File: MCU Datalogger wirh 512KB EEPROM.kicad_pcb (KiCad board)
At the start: 2 copper layers, 56.3 x 48.7 mm, 30 parts, among them IC1 ATMEGA328P-AU, J1 Conn_01x04_Pin, J2 Conn_01x04_Pin, J3 Conn_01x09_Pin, J4 Conn_02x03_Odd_Even, U1 24LC1025, U2 24LC1025, U3 DS1137S+, Y1 16 MHz, Y2 32.768 KHz

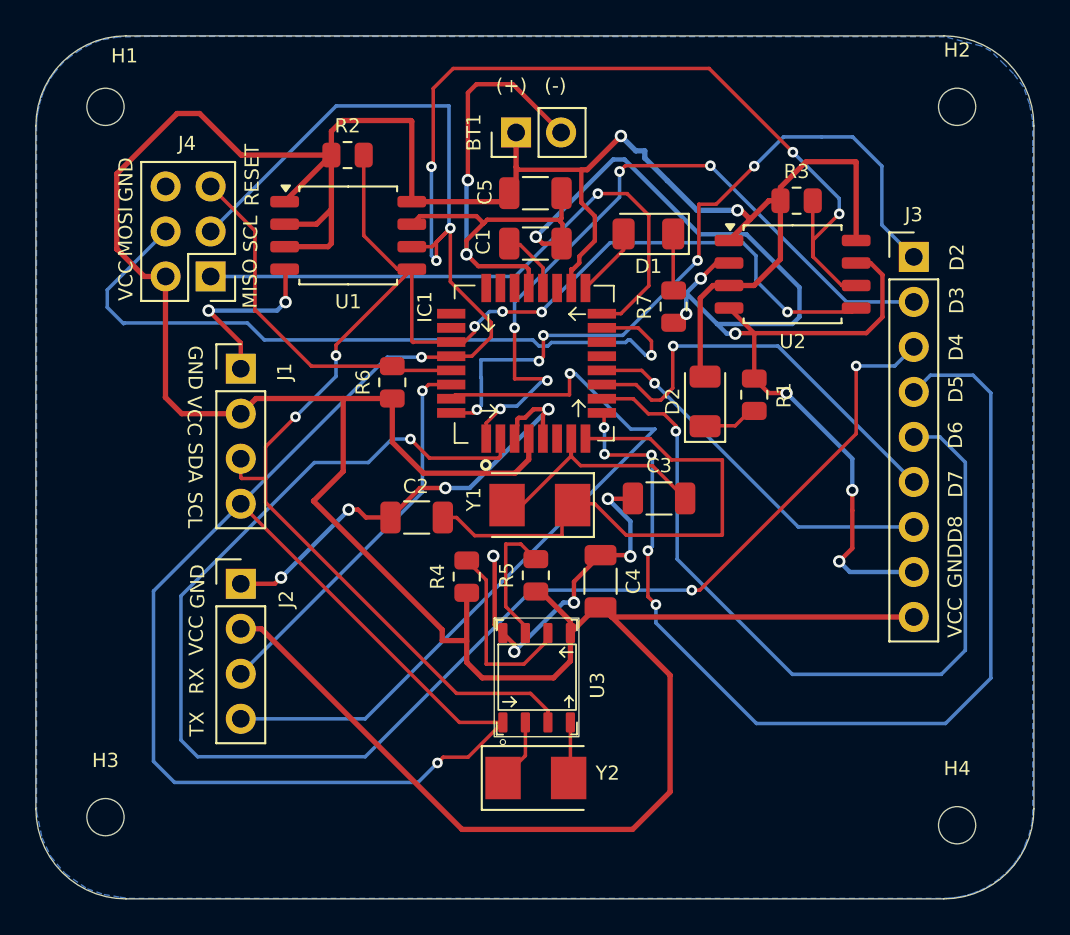
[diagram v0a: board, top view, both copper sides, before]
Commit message: Included values for assembly.
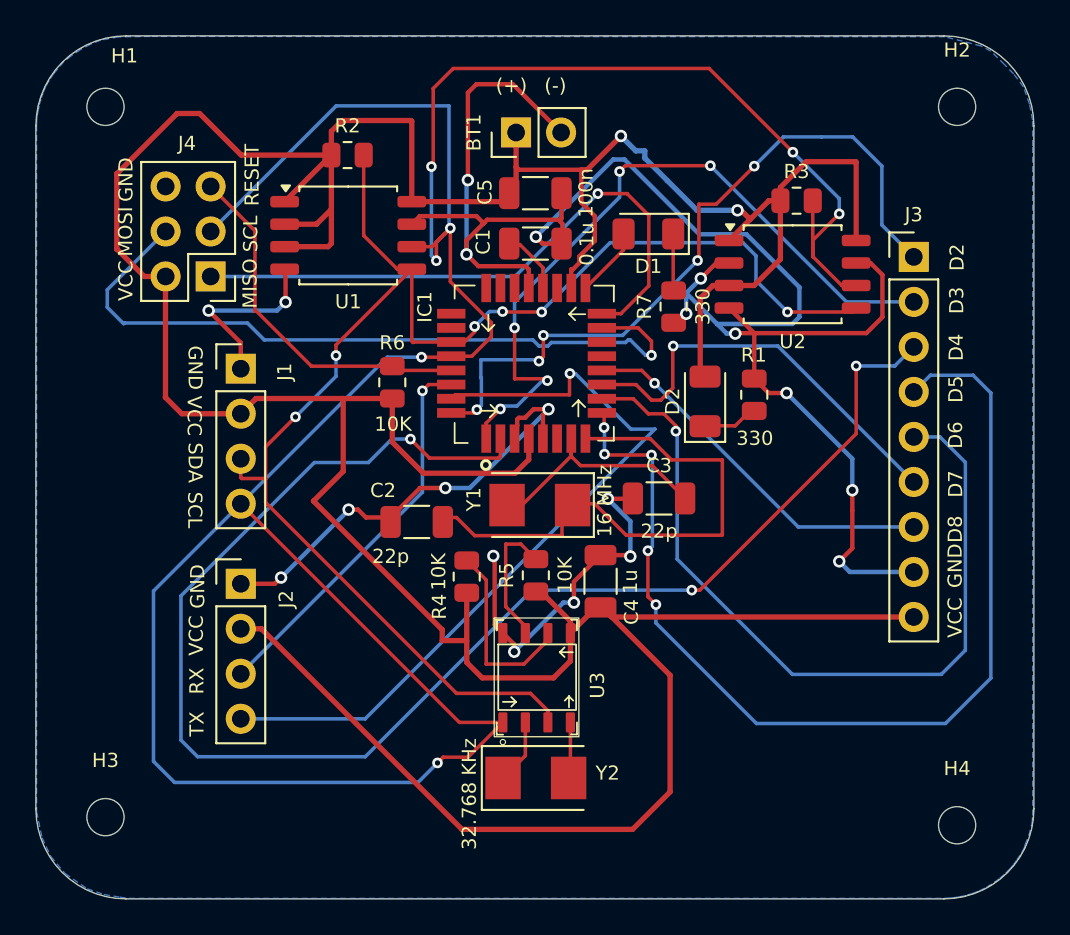
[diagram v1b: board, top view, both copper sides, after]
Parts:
- moved C2 0.25 mm to (129.2, 102.1)
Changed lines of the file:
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@@
 		)
 		(property "Value" "100n"
-			(at 0 1.85 0)
-			(layer "F.Fab")
+			(at 2.8515 -0.0171 90)
+			(layer "F.SilkS")
 			(effects
 				(font
-					(size 1 1)
+					(size 0.8 0.8)
 					(thickness 0.15)
 				)
@@
 		)
 		(property "Value" "16 MHz"
-			(at 0 2.8 0)
-			(layer "F.Fab")
+			(at -3.6615 0.2371 90)
+			(layer "F.SilkS")
 			(effects
 				(font
-					(size 1 1)
+					(size 0.8 0.8)
 					(thickness 0.15)
 				)
@@
 		(property "Value" "330"
 			(at 0 1.65 90)
-			(layer "F.Fab")
+			(layer "F.SilkS")
 			(effects
 				(font
-					(size 1 1)
+					(size 0.8 0.8)
 					(thickness 0.15)
 				)
@@
 		(tags "resistor")
 		(property "Reference" "R4"
-			(at 0 -1.65 90)
+			(at -1.6954 -1.5435 90)
 			(layer "F.SilkS")
 			(effects
@@
 		)
 		(property "Value" "10K"
-			(at 0 1.65 90)
-			(layer "F.Fab")
+			(at 0.2746 -1.5835 90)
+			(layer "F.SilkS")
 			(effects
 				(font
-					(size 1 1)
+					(size 0.8 0.8)
 					(thickness 0.15)
 				)
@@
 		(tags "capacitor")
 		(property "Reference" "C4"
-			(at 0 -1.85 90)
+			(at 1.7329 -1.7465 90)
 			(layer "F.SilkS")
 			(effects
@@
 		)
 		(property "Value" "1u"
-			(at 0 1.85 90)
-			(layer "F.Fab")
+			(at 0.0229 -1.6865 90)
+			(layer "F.SilkS")
 			(effects
 				(font
-					(size 1 1)
+					(size 0.8 0.8)
 					(thickness 0.15)
 				)
@@
 		(tags "resistor")
 		(property "Reference" "R6"
-			(at 0 -1.65 90)
+			(at 2.2321 -0.0035 180)
 			(layer "F.SilkS")
 			(effects
@@
 		)
 		(property "Value" "10K"
-			(at 0 1.65 90)
-			(layer "F.Fab")
+			(at -2.3579 0.0465 180)
+			(layer "F.SilkS")
 			(effects
 				(font
-					(size 1 1)
+					(size 0.8 0.8)
 					(thickness 0.15)
 				)
@@
 		)
 		(property "Value" "32.768 KHz"
-			(at 0 2.8 0)
-			(layer "F.Fab")
+			(at -3.7535 0.9029 90)
+			(layer "F.SilkS")
 			(effects
 				(font
-					(size 1 1)
+					(size 0.8 0.8)
 					(thickness 0.15)
 				)
@@
 		(property "Value" "22p"
 			(at 0 1.85 0)
-			(layer "F.Fab")
+			(layer "F.SilkS")
 			(effects
 				(font
-					(size 1 1)
+					(size 0.8 0.8)
 					(thickness 0.15)
 				)
@@
 	(footprint "Capacitor_SMD:C_1206_3216Metric"
 		(layer "F.Cu")
-		(at 129.2185 101.8871)
+		(at 129.22 102.14)
 		(descr "Capacitor SMD 1206 (3216 Metric), square (rectangular) end terminal, IPC-7351 nominal, (Body size source: IPC-SM-782 page 76, https://www.pcb-3d.com/wordpress/wp-content/uploads/ipc-sm-782a_amendment_1_and_2.pdf), generated with kicad-footprint-generator")
 		(tags "capacitor")
 		(property "Reference" "C2"
-			(at -0.05 -1.75 0)
+			(at -1.8985 -1.7771 0)
 			(layer "F.SilkS")
 			(effects
@@
 		)
 		(property "Value" "22p"
-			(at 0 1.85 0)
-			(layer "F.Fab")
+			(at -1.4685 1.9429 0)
+			(layer "F.SilkS")
 			(effects
 				(font
-					(size 1 1)
+					(size 0.8 0.8)
 					(thickness 0.15)
 				)
@@
 		(property "Value" "10K"
 			(at 0 1.65 90)
-			(layer "F.Fab")
+			(layer "F.SilkS")
 			(effects
 				(font
-					(size 1 1)
+					(size 0.8 0.8)
 					(thickness 0.15)
 				)
@@
 		(tags "resistor")
 		(property "Reference" "R1"
-			(at -0.025 1.675 270)
+			(at 2.2421 -0.0285 0)
 			(layer "F.SilkS")
 			(effects
@@
 		)
 		(property "Value" "330"
-			(at 0 1.65 90)
-			(layer "F.Fab")
+			(at -2.4579 0.0315 180)
+			(layer "F.SilkS")
 			(effects
 				(font
-					(size 1 1)
+					(size 0.8 0.8)
 					(thickness 0.15)
 				)
@@
 		)
 		(property "Value" "0.1u"
-			(at 0 1.85 0)
-			(layer "F.Fab")
+			(at 2.9011 0.0289 90)
+			(layer "F.SilkS")
 			(effects
 				(font
-					(size 1 1)
+					(size 0.8 0.8)
 					(thickness 0.15)
 				)
@@
 	)
 	(segment
-		(start 129.3989 84.8817)
-		(end 132.5915 84.8817)
+		(start 129.4073 100.2233)
+		(end 130.8389 100.2233)
 		(width 0.25)
 		(layer "F.Cu")
@@
 	)
 	(segment
-		(start 126.3559 101.8871)
-		(end 127.7435 101.8871)
+		(start 129.3989 84.8817)
+		(end 132.5915 84.8817)
 		(width 0.25)
 		(layer "F.Cu")
@@
 	)
 	(segment
+		(start 127.745 101.8856)
+		(end 129.4073 100.2233)
+		(width 0.25)
+		(layer "F.Cu")
+		(net 1)
+	)
+	(segment
 		(start 149.0828 94.8639)
 		(end 148.2685 94.0496)
@@
 	)
 	(segment
-		(start 119.2935 93.4921)
-		(end 119.2935 92.0271)
+		(start 125.9113 101.4425)
+		(end 126.3559 101.8871)
 		(width 0.25)
 		(layer "F.Cu")
@@
 	)
 	(segment
-		(start 132.5915 84.8817)
-		(end 132.9979 85.2881)
+		(start 119.2935 93.4921)
+		(end 119.2935 92.0271)
 		(width 0.25)
 		(layer "F.Cu")
@@
 	)
 	(segment
-		(start 127.7435 101.8871)
-		(end 129.4073 100.2233)
+		(start 132.5915 84.8817)
+		(end 132.9979 85.2881)
 		(width 0.25)
 		(layer "F.Cu")
@@
 	)
 	(segment
-		(start 125.9113 101.4425)
-		(end 126.3559 101.8871)
-		(width 0.25)
-		(layer "F.Cu")
-		(net 1)
-	)
-	(segment
 		(start 139.5935 104.0121)
 		(end 141.2063 104.0121)
@@
 	)
 	(segment
-		(start 125.3779 101.4425)
-		(end 125.9113 101.4425)
-		(width 0.25)
-		(layer "F.Cu")
-		(net 1)
-	)
-	(segment
 		(start 146.1259 87.5271)
 		(end 146.8435 87.5271)
@@
 	)
 	(segment
-		(start 129.4073 100.2233)
-		(end 130.8389 100.2233)
+		(start 127.745 102.14)
+		(end 127.745 101.8856)
 		(width 0.25)
 		(layer "F.Cu")
@@
 	)
 	(segment
+		(start 126.3559 101.8871)
+		(end 127.4921 101.8871)
+		(width 0.25)
+		(layer "F.Cu")
+		(net 1)
+	)
+	(segment
 		(start 133.6195 104.1347)
 		(end 133.5435 104.0587)
@@
 	)
 	(segment
+		(start 125.3779 101.4425)
+		(end 125.9113 101.4425)
+		(width 0.25)
+		(layer "F.Cu")
+		(net 1)
+	)
+	(segment
 		(start 121.8219 87.9305)
 		(end 121.7685 87.8771)
@@
 	)
 	(segment
+		(start 127.4921 101.8871)
+		(end 127.745 102.14)
+		(width 0.25)
+		(layer "F.Cu")
+		(net 1)
+	)
+	(segment
 		(start 143.7185 90.8996)
 		(end 143.9218 90.8996)
@@
 	)
 	(segment
-		(start 137.7185 101.1371)
-		(end 137.7435 101.1121)
+		(start 130.9479 101.8871)
+		(end 131.4685 101.8871)
 		(width 0.2)
 		(layer "F.Cu")
@@
 	)
 	(segment
-		(start 137.4185 102.9121)
-		(end 137.4185 101.2371)
+		(start 143.5935 98.6371)
+		(end 142.3935 97.4371)
 		(width 0.2)
 		(layer "F.Cu")
@@
 	)
 	(segment
-		(start 137.5185 101.1371)
-		(end 137.7185 101.1371)
+		(start 138.0185 101.1871)
+		(end 138.0935 101.1121)
 		(width 0.2)
 		(layer "F.Cu")
@@
 	)
 	(segment
-		(start 143.5935 98.6371)
-		(end 142.3935 97.4371)
+		(start 146.4685 98.6371)
+		(end 143.5935 98.6371)
 		(width 0.2)
 		(layer "F.Cu")
@@
 	)
 	(segment
-		(start 138.0185 101.1871)
-		(end 138.0935 101.1121)
+		(start 137.7435 101.1121)
+		(end 137.9435 101.1121)
 		(width 0.2)
 		(layer "F.Cu")
@@
 	)
 	(segment
-		(start 146.4685 98.6371)
-		(end 143.5935 98.6371)
+		(start 137.7185 101.1371)
+		(end 137.7435 101.1121)
 		(width 0.2)
 		(layer "F.Cu")
@@
 	)
 	(segment
-		(start 137.4185 101.2371)
-		(end 137.5185 101.1371)
+		(start 132.4935 102.9121)
+		(end 137.4185 102.9121)
 		(width 0.2)
 		(layer "F.Cu")
@@
 	)
 	(segment
+		(start 137.4185 102.9121)
+		(end 137.4185 101.2371)
+		(width 0.2)
+		(layer "F.Cu")
+		(net 4)
+	)
+	(segment
 		(start 146.4685 102.8621)
 		(end 146.4685 98.6371)
@@
 	)
 	(segment
-		(start 137.9435 101.1121)
-		(end 138.0185 101.1871)
+		(start 131.4685 101.8871)
+		(end 132.4935 102.9121)
 		(width 0.2)
 		(layer "F.Cu")
@@
 	)
 	(segment
-		(start 130.6935 101.8871)
-		(end 131.4685 101.8871)
+		(start 138.2435 100.8121)
+		(end 137.9685 101.0871)
 		(width 0.2)
 		(layer "F.Cu")
@@
 	)
 	(segment
-		(start 132.4935 102.9121)
-		(end 137.4185 102.9121)
+		(start 137.9435 101.1121)
+		(end 138.0185 101.1871)
 		(width 0.2)
 		(layer "F.Cu")
@@
 	)
 	(segment
-		(start 138.2435 100.8121)
-		(end 137.9685 101.0871)
+		(start 130.695 102.14)
+		(end 130.9479 101.8871)
 		(width 0.2)
 		(layer "F.Cu")
@@
 	)
 	(segment
-		(start 137.9685 101.1371)
-		(end 138.0185 101.1871)
+		(start 137.4185 101.2371)
+		(end 137.5185 101.1371)
 		(width 0.2)
 		(layer "F.Cu")
@@
 	)
 	(segment
-		(start 131.4685 101.8871)
-		(end 132.4935 102.9121)
+		(start 137.9685 101.1371)
+		(end 138.0185 101.1871)
 		(width 0.2)
 		(layer "F.Cu")
@@
 	)
 	(segment
-		(start 137.7435 101.1121)
-		(end 137.9435 101.1121)
+		(start 137.5185 101.1371)
+		(end 137.7185 101.1371)
 		(width 0.2)
 		(layer "F.Cu")

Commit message: Done more improvements for the placements in front silkscreen.
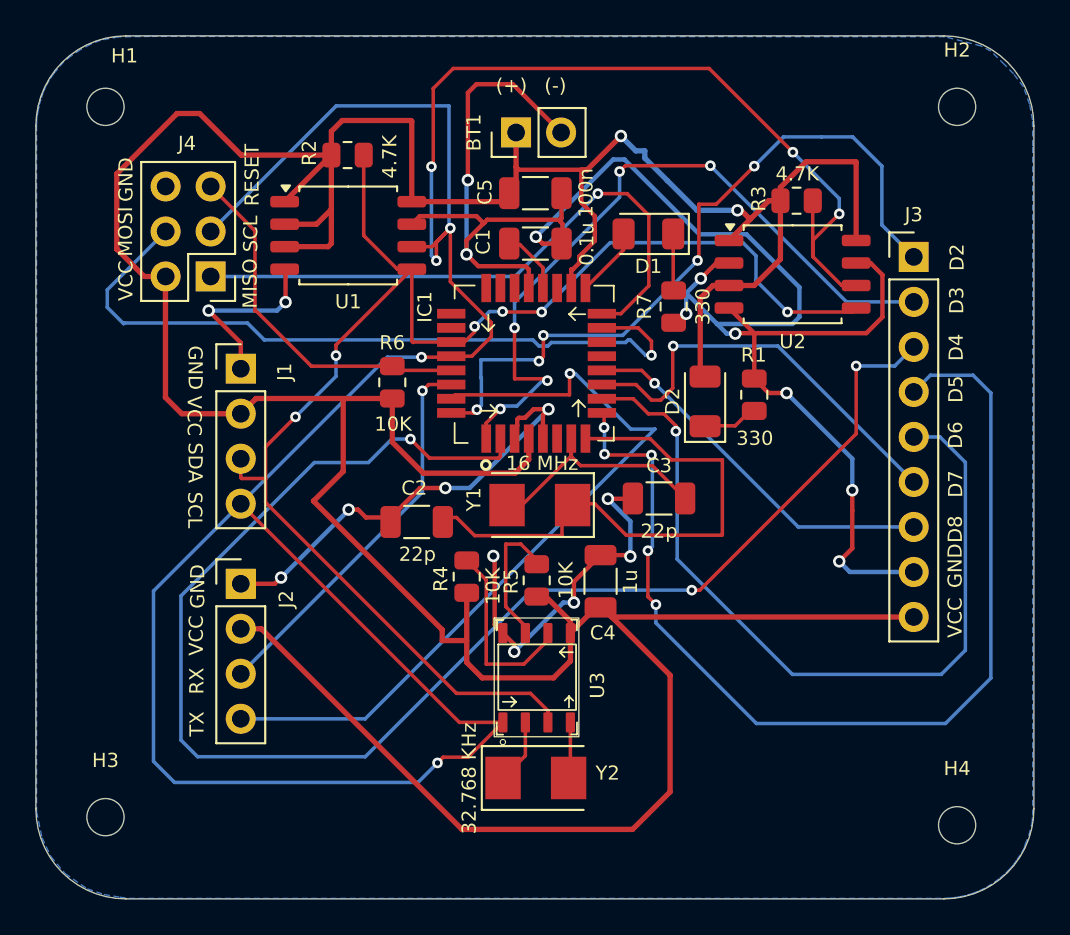
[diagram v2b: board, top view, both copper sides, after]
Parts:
- moved R5 0.29 mm to (136.0, 105.4)
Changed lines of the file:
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@@
 		)
 		(property "Value" "16 MHz"
-			(at -3.6615 0.2371 90)
+			(at -0.1279 2.3557 180)
 			(layer "F.SilkS")
 			(effects
@@
 		(tags "resistor")
 		(property "Reference" "R4"
-			(at -1.6954 -1.5435 90)
+			(at -0.1254 -1.4635 90)
 			(layer "F.SilkS")
 			(effects
@@
 		)
 		(property "Value" "10K"
-			(at 0.2746 -1.5835 90)
+			(at -0.541 1.4843 90)
 			(layer "F.SilkS")
 			(effects
@@
 		(tags "capacitor")
 		(property "Reference" "C4"
-			(at 1.7329 -1.7465 90)
+			(at 2.9129 -0.1265 180)
 			(layer "F.SilkS")
 			(effects
@@
 		)
 		(property "Value" "32.768 KHz"
-			(at -3.7535 0.9029 90)
+			(at -3.7619 0.0243 90)
 			(layer "F.SilkS")
 			(effects
@@
 		(tags "capacitor")
 		(property "Reference" "C2"
-			(at -1.8985 -1.7771 0)
+			(at -0.1372 -1.9116 0)
 			(layer "F.SilkS")
 			(effects
@@
 		)
 		(property "Value" "22p"
-			(at -1.4685 1.9429 0)
+			(at 0.0406 1.8222 0)
 			(layer "F.SilkS")
 			(effects
@@
 	(footprint "Resistor_SMD:R_0805_2012Metric"
 		(layer "F.Cu")
-		(at 135.9435 105.1496 90)
+		(at 135.9916 105.4354 90)
 		(descr "Resistor SMD 0805 (2012 Metric), square (rectangular) end terminal, IPC-7351 nominal, (Body size source: IPC-SM-782 page 72, https://www.pcb-3d.com/wordpress/wp-content/uploads/ipc-sm-782a_amendment_1_and_2.pdf), generated with kicad-footprint-generator")
 		(tags "resistor")
 		(property "Reference" "R5"
-			(at 0 -1.65 90)
+			(at -0.0504 -1.4435 90)
 			(layer "F.SilkS")
 			(effects
@@
 		(tags "resistor")
 		(property "Reference" "R3"
-			(at 0 -1.65 0)
+			(at -2.136 -0.1121 90)
 			(layer "F.SilkS")
 			(effects
@@
 		)
 		(property "Value" "4.7K"
-			(at 0 1.65 0)
-			(layer "F.Fab")
+			(at 0.0422 -1.5129 180)
+			(layer "F.SilkS")
 			(effects
 				(font
-					(size 1 1)
+					(size 0.8 0.8)
 					(thickness 0.15)
 				)
@@
 		(tags "resistor")
 		(property "Reference" "R2"
-			(at 0 -1.65 0)
+			(at -2.1585 -0.1171 90)
 			(layer "F.SilkS")
 			(effects
@@
 		)
 		(property "Value" "4.7K"
-			(at 0 1.65 0)
-			(layer "F.Fab")
+			(at 2.3815 0.0929 90)
+			(layer "F.SilkS")
 			(effects
 				(font
-					(size 1 1)
+					(size 0.8 0.8)
 					(thickness 0.15)
 				)
@@
 	)
 	(segment
-		(start 137.8935 107.7371)
-		(end 136.2185 106.0621)
-		(width 0.3)
-		(layer "F.Cu")
-		(net 2)
-	)
-	(segment
 		(start 124.406 81.4371)
 		(end 124.3985 81.4371)
@@
 	)
 	(segment
+		(start 137.8935 107.7371)
+		(end 136.5043 106.3479)
+		(width 0.3)
+		(layer "F.Cu")
+		(net 2)
+	)
+	(segment
 		(start 138.035926 87.8849)
 		(end 138.3957 87.525126)
@@
 	)
 	(segment
+		(start 137.8935 108.4096)
+		(end 137.8935 107.7371)
+		(width 0.3)
+		(layer "F.Cu")
+		(net 2)
+	)
+	(segment
 		(start 125.0731 99.2835)
 		(end 123.3967 100.9599)
@@
 	)
 	(segment
-		(start 139.5935 106.9621)
-		(end 139.5935 106.8871)
+		(start 136.5043 106.3479)
+		(end 135.9916 106.3479)
 		(width 0.3)
 		(layer "F.Cu")
@@
 	)
 	(segment
-		(start 119.3171 81.4371)
-		(end 124.406 81.4371)
+		(start 139.5935 106.9621)
+		(end 139.5935 106.8871)
 		(width 0.3)
 		(layer "F.Cu")
@@
 	)
 	(segment
-		(start 136.2185 106.0621)
-		(end 135.9435 106.0621)
+		(start 119.3171 81.4371)
+		(end 124.406 81.4371)
 		(width 0.3)
 		(layer "F.Cu")
@@
 	)
 	(segment
-		(start 137.8935 108.4096)
-		(end 137.8935 107.7371)
-		(width 0.3)
-		(layer "F.Cu")
-		(net 2)
-	)
-	(segment
 		(start 124.406 86.4246)
 		(end 124.406 84.4996)
@@
 	)
 	(segment
-		(start 135.0935 103.3871)
-		(end 134.2435 103.3871)
+		(start 135.3535 108.0221)
+		(end 135.3535 108.4096)
 		(width 0.2)
 		(layer "F.Cu")
@@
 	)
 	(segment
-		(start 135.9435 104.2371)
-		(end 135.0935 103.3871)
+		(start 134.2435 103.3871)
+		(end 134.2435 106.9121)
 		(width 0.2)
 		(layer "F.Cu")
@@
 	)
 	(segment
-		(start 135.3535 108.0221)
-		(end 135.3535 108.4096)
+		(start 135.9916 104.5229)
+		(end 135.9916 104.2852)
 		(width 0.2)
 		(layer "F.Cu")
@@
 	)
 	(segment
-		(start 134.2435 103.3871)
-		(end 134.2435 106.9121)
+		(start 134.2435 106.9121)
+		(end 135.3535 108.0221)
 		(width 0.2)
 		(layer "F.Cu")
@@
 	)
 	(segment
-		(start 134.2435 106.9121)
-		(end 135.3535 108.0221)
+		(start 135.9916 104.2852)
+		(end 135.0935 103.3871)
+		(width 0.2)
+		(layer "F.Cu")
+		(net 33)
+	)
+	(segment
+		(start 135.0935 103.3871)
+		(end 134.2435 103.3871)
 		(width 0.2)
 		(layer "F.Cu")
